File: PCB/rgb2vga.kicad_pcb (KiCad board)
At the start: 2 copper layers, 73.7 x 55.9 mm, 41 parts, among them J1 GPIO_0, J2 RGB_IN, J3 COCO3_RGB_IN, J4 C_VIDEO_IN, J5 GPIO_1, J6 VGA_OUT, SW1 SW_DIP_x08, U1 LM1881

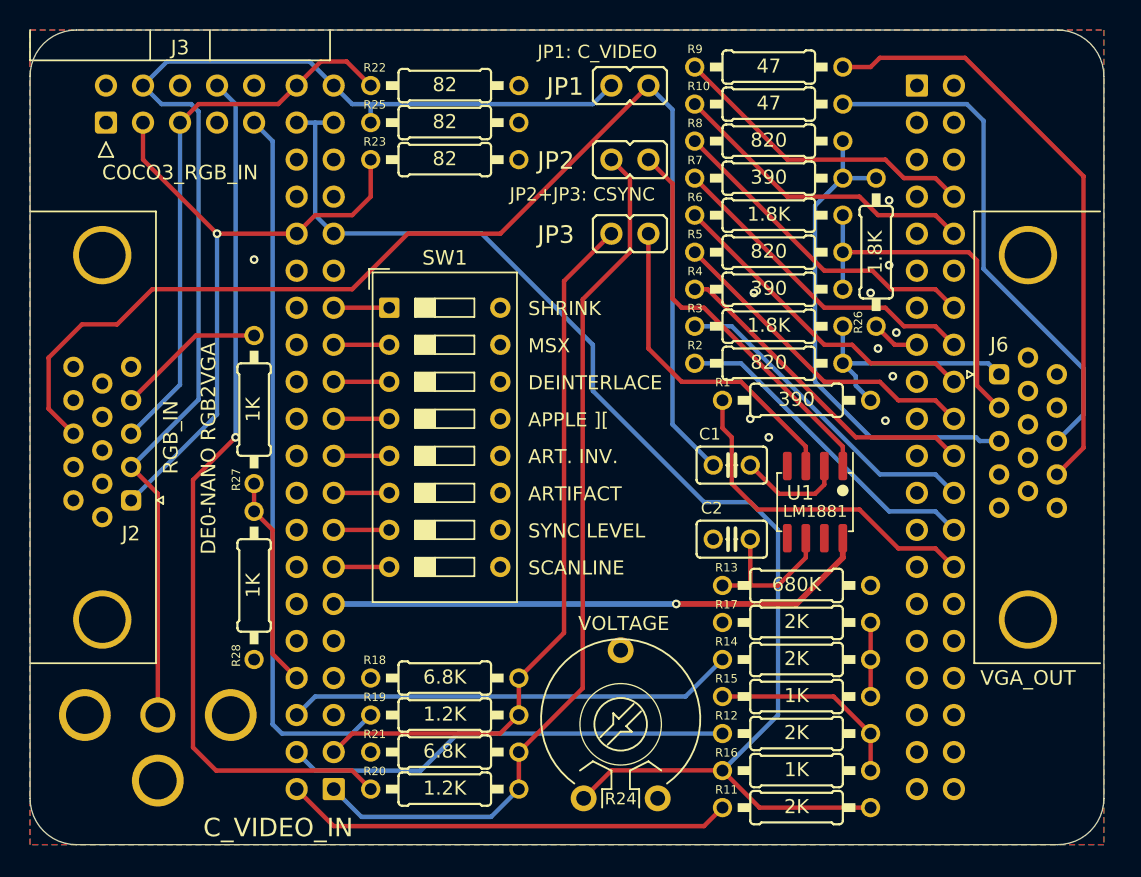
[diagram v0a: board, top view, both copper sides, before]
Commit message: rearrange R22 R25
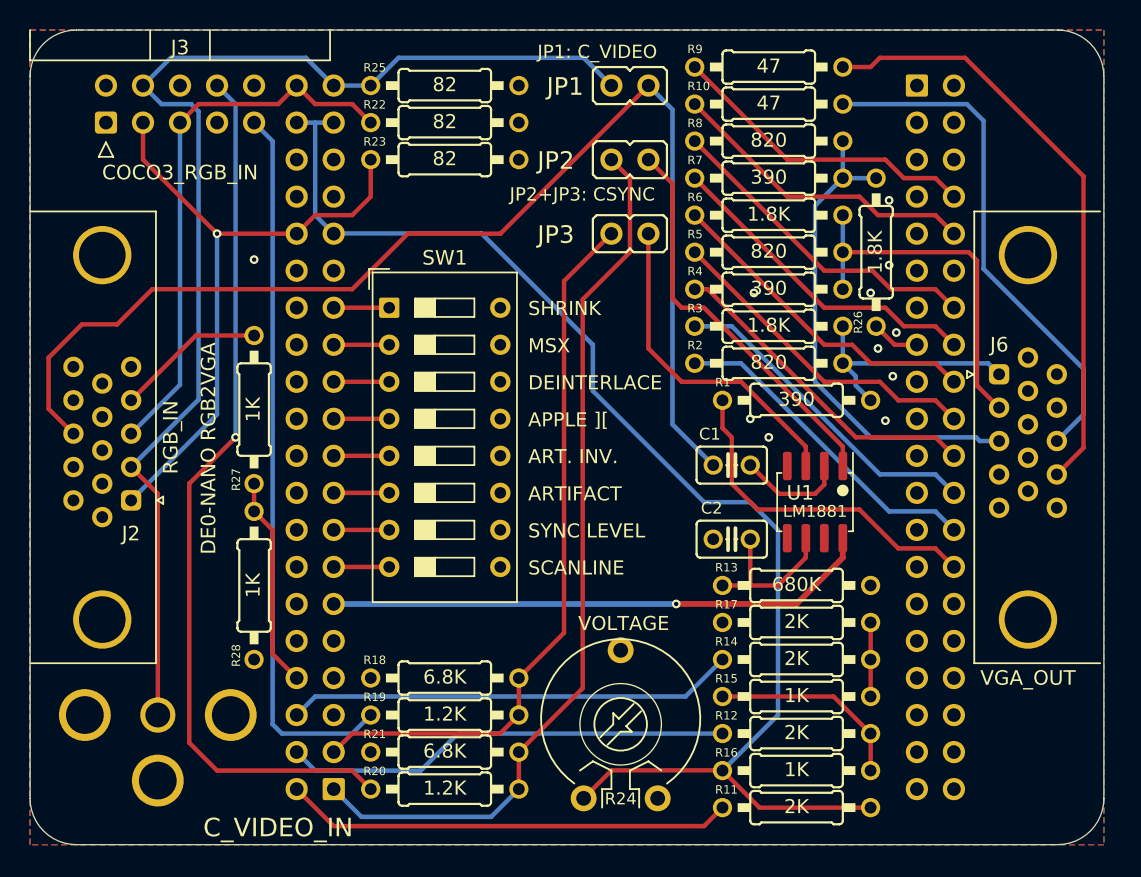
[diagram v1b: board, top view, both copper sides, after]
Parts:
- moved R22 2.54 mm to (130.8, 79.4)
- moved R25 2.54 mm to (130.8, 76.8)
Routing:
- net /DIFFG: track 84.4 -> 83.9 mm

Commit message: better 3d model for vga connector
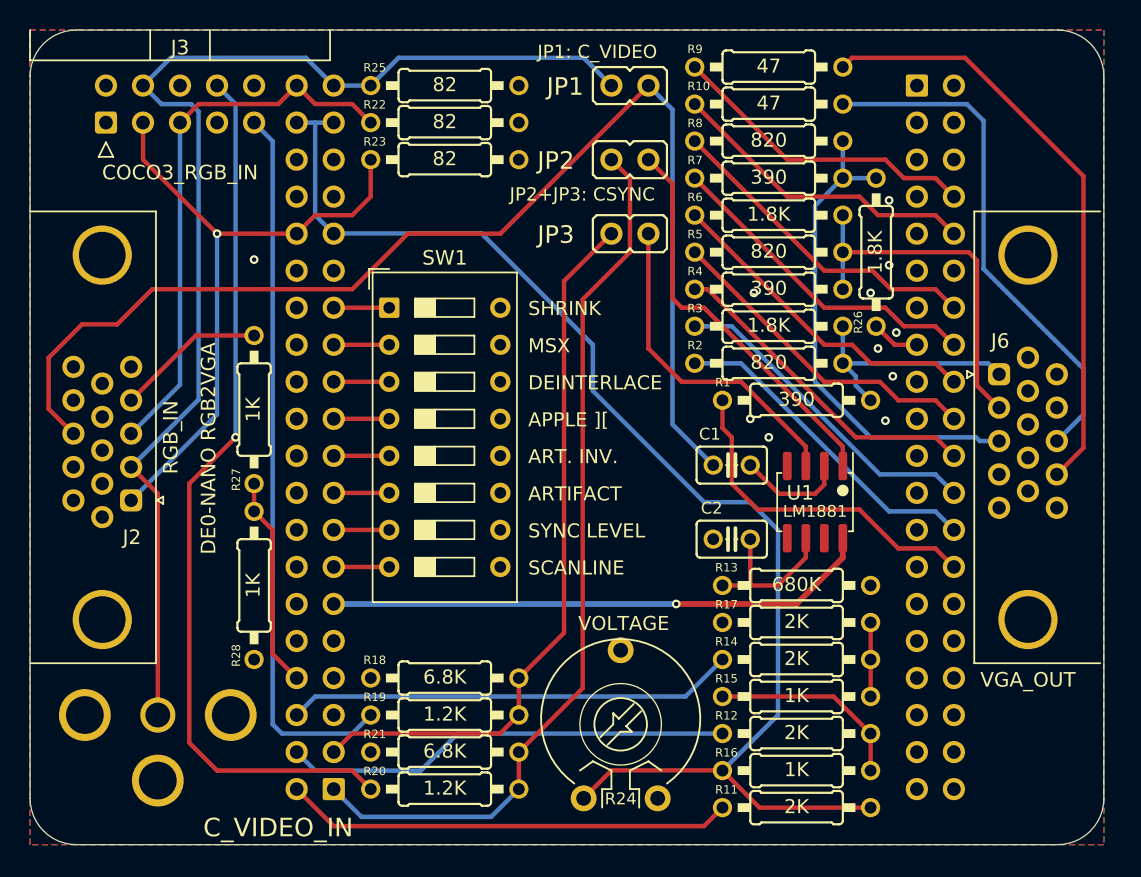
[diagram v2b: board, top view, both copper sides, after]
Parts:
- J2, J6: footprint 000_LOCAL:DE15F_Horiz_P2.29x1.98_3.03mm -> 000_LOCAL:HD15-SN-25

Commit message: move R26
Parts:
- moved R26 9.37 mm to (154.9, 80.6), turned to 0 degrees
- moved R3 3.18 mm to (154.9, 95.9)
- moved R5 3.18 mm to (154.9, 90.8)
- moved R6 3.18 mm to (154.9, 88.3)
- moved R8 3.18 mm to (154.9, 83.2)
- moved R2 3.17 mm to (154.9, 98.4)
- moved R4 3.17 mm to (154.9, 93.3)
- moved R7 3.17 mm to (154.9, 85.7)
- moved R1 2.54 mm to (154.9, 101.0)
- moved R10 1.91 mm to (154.9, 78.1)
- moved R9 1.91 mm to (154.9, 75.6)
- moved C1 1.80 mm to (151.8, 104.1)
- moved U1 1.37 mm to (157.4, 106.2)
- moved C2 1.27 mm to (151.8, 108.0)
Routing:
- net /B0: track 3.32 -> 27.6 mm
- net /DIFF_N: track 91.1 -> 87.6 mm
- net /G1: track 22.5 -> 19.6 mm
- net /G0: track 22.5 -> 19.6 mm
- net /B1: track 22.5 -> 19.6 mm
- net /B2: track 22.5 -> 19.6 mm
- net /G2: track 22.5 -> 19.6 mm
- net /R0: track 22.5 -> 19.6 mm
- net /R1: track 22.5 -> 19.6 mm
- net /R2: track 23.6 -> 20.7 mm
- net /RED: track 16.9 -> 14.6 mm, vias 0 -> 1
- net /HS: track 21.5 -> 19.6 mm
- net /GREEN: track 25.2 -> 23.3 mm
- net /VS: track 21.5 -> 19.6 mm
- net Net-(JP2-Pad1): track 27.4 -> 29.3 mm
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
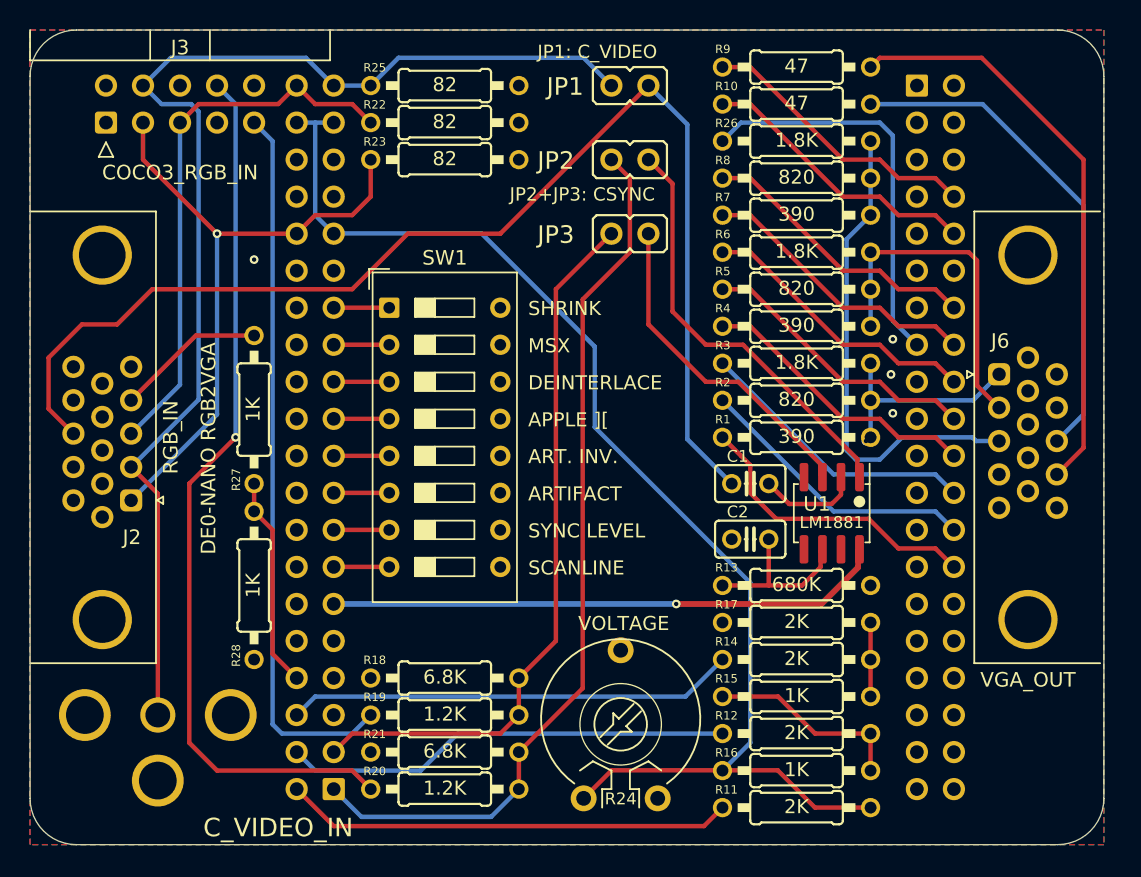
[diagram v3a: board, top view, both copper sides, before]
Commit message: fix spacing between GPIO0 and GPIO1
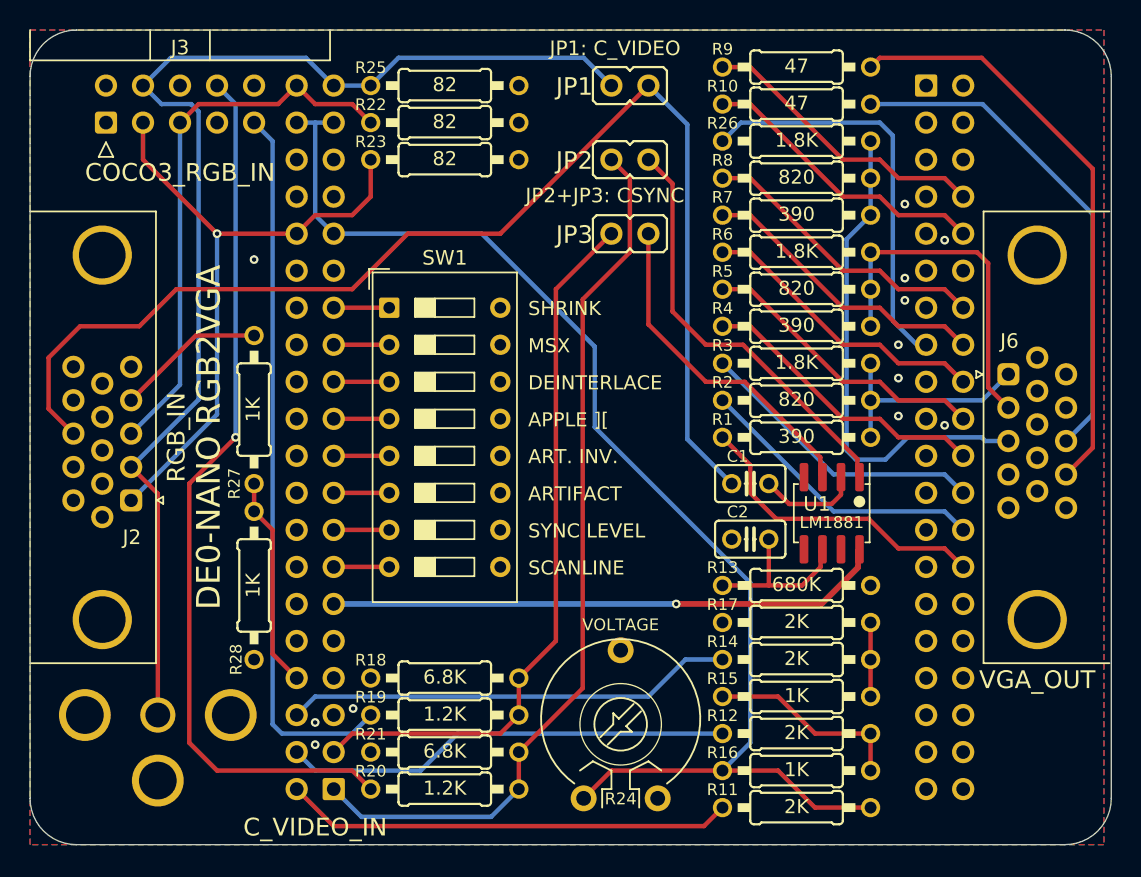
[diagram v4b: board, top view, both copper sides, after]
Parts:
- moved J5 0.64 mm to (163.8, 76.8)
- moved J6 0.63 mm to (171.4, 101.0)
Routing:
- net /HS: track 19.6 -> 20.2 mm
- net /VS: track 19.6 -> 20.2 mm
- net /RED: track 14.6 -> 15.3 mm, vias 1 -> 0
- net /R2: track 20.7 -> 21.3 mm
- net /R1: track 19.6 -> 20.2 mm
- net /R0: track 19.6 -> 20.2 mm
- net /G2: track 19.6 -> 20.2 mm
- net /G1: track 19.6 -> 20.2 mm
- net /G0: track 19.6 -> 20.2 mm
- net /B2: track 19.6 -> 20.2 mm
- net /B1: track 19.6 -> 20.2 mm
- net /BLUE: track 33.4 -> 34.0 mm
- net /GREEN: track 23.3 -> 23.9 mm
- net GND: vias 4 -> 12
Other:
- board size 73.7 x 55.9 mm -> 74.2 x 55.9 mm
- board text added: "Based on FPGA RGB2VGA by Luis Antoniosi"
- board text removed: "Original Design 2014 Luis Antoniosi"
